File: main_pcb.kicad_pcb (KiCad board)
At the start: 2 copper layers, 56 parts, among them J1 STLink_conn, J10 Conn_01x03_Male, J11 Conn_02x02_Odd_Even, J12 Conn_01x09_Male, J13 Conn_Coaxial, J14 Conn_01x03_Male, J15 USB_conn, J2 Conn_01x04_Male, J3 Conn_02x03_Odd_Even, J4 Conn_02x03_Odd_Even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

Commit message: initial commit
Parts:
- C1, C6, C7, C8, C9: footprint Capacitors_SMD:C_0805_HandSoldering -> LoraWAN_pcb:C_0805_HandSoldering
- C2, C3, C4, C5: footprint Capacitors_SMD:C_0805_HandSoldering -> LoraWAN_pcb:C_0805_HandSoldering; moved to F.Cu
- D1, D3, D4, D5: footprint LEDs:LED_0805_HandSoldering -> LoraWAN_pcb:LED_0805_HandSoldering
- D2: footprint RHF78_footprint:RHF78_052 -> LoraWAN_pcb:RHF78_052
- J1: footprint Pin_Headers:Pin_Header_Straight_1x05_Pitch2.54mm -> LoraWAN_pcb:Pin_Header_Straight_1x05_Pitch2.54mm
- J10, J14, J6, J7: footprint Pin_Headers:Pin_Header_Straight_1x03_Pitch2.54mm -> LoraWAN_pcb:Pin_Header_Straight_1x03_Pitch2.54mm
- J11: footprint Pin_Headers:Pin_Header_Straight_2x02_Pitch2.54mm -> LoraWAN_pcb:Pin_Header_Straight_2x02_Pitch2.54mm
- J12: footprint Pin_Headers:Pin_Header_Straight_1x09_Pitch2.54mm -> LoraWAN_pcb:Pin_Header_Straight_1x09_Pitch2.54mm
- J13: footprint U_FL_smd:U_FL_smd -> LoraWAN_pcb:U_FL_smd
- J15: footprint Connectors:USB_Micro-B -> LoraWAN_pcb:USB_Micro-B
- J2: footprint Pin_Headers:Pin_Header_Straight_1x04_Pitch2.54mm -> LoraWAN_pcb:Pin_Header_Straight_1x04_Pitch2.54mm
- J3, J4: footprint Pin_Headers:Pin_Header_Straight_2x03_Pitch2.54mm -> LoraWAN_pcb:Pin_Header_Straight_2x03_Pitch2.54mm
- J5, J9: footprint Pin_Headers:Pin_Header_Straight_1x01_Pitch2.54mm -> LoraWAN_pcb:Pin_Header_Straight_1x01_Pitch2.54mm
- J8: footprint Pin_Headers:Pin_Header_Straight_1x06_Pitch2.54mm -> LoraWAN_pcb:Pin_Header_Straight_1x06_Pitch2.54mm
- R1, R10, R11, R12, R13, R16, R18, R19, R2, R3, R4, R5, R8, R9: footprint Resistors_SMD:R_0805_HandSoldering -> LoraWAN_pcb:R_0805_HandSoldering
- R14, R15, R6, R7: footprint Resistors_SMD:R_0805_HandSoldering -> LoraWAN_pcb:R_0805_HandSoldering; moved to F.Cu
- R17: footprint Potentiometers:Potentiometer_Trimmer_Bourns_3296W -> LoraWAN_pcb:Potentiometer_Trimmer_Bourns_3296W
- SW1, SW2: footprint Buttons_Switches_SMD:SW_SPST_EVQPE1 -> LoraWAN_pcb:SW_SPST_EVQPE1
- U1: footprint Housings_QFP:LQFP-48_7x7mm_Pitch0.5mm -> LoraWAN_pcb:LQFP-48_7x7mm_Pitch0.5mm; moved to F.Cu
- U2: footprint Housings_SOIC:SOIC-8_3.9x4.9mm_Pitch1.27mm -> LoraWAN_pcb:SOIC-8_3.9x4.9mm_Pitch1.27mm; moved to F.Cu
- U3: footprint TO_SOT_Packages_SMD:SOT-23-6_Handsoldering -> LoraWAN_pcb:SOT-23-6_Handsoldering
- U4: footprint TO_SOT_Packages_SMD:SOT-223-3_TabPin2 -> LoraWAN_pcb:SOT-223-3_TabPin2
- Y1: footprint Crystals:Crystal_HC18-U_Vertical -> LoraWAN_pcb:Crystal_HC18-U_Vertical
- Y2: footprint Crystals:Crystal_AT310_d3.0mm_l10.0mm_Vertical -> LoraWAN_pcb:Crystal_AT310_d3.0mm_l10.0mm_Vertical
- moved Y2 74.5 mm to (174.2, 81.7), turned to 0 degrees
- moved C4 67.8 mm to (170.1, 83.4)
- moved C2 67.2 mm to (170.1, 80.6), turned to 0 degrees
- moved U3 65.3 mm to (107.3, 102.3)
- moved C5 63.2 mm to (163.7, 90.3)
- moved R15 61.4 mm to (175.5, 72.0), turned to 0 degrees
- moved C3 58.3 mm to (159.4, 94.5), turned to 0 degrees
- moved R2 55.3 mm to (158.1, 88.8), turned to 0 degrees
- moved R6 54.7 mm to (169.7, 72.0), turned to 0 degrees
- moved R4 49.6 mm to (169.7, 77.7), turned to 0 degrees
- moved J3 44.9 mm to (150.3, 86.2), turned to 0 degrees
- moved R7 44.4 mm to (158.1, 85.9), turned to 0 degrees
- moved J1 43.4 mm to (138.5, 65.0), turned to 0 degrees
- moved J13 42.9 mm to (125.6, 101.6)
- moved J6 41.6 mm to (147.8, 76.5)
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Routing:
- net GND: track 102.2 -> 0.00 mm, vias 3 -> 0
- net VCC: track 59.6 -> 0.00 mm
- net Net-(J2-Pad3): track 49.7 -> 0.00 mm
- net Net-(J2-Pad2): track 46.1 -> 0.00 mm
- net Net-(D2-Pad23): track 38.2 -> 0.00 mm, vias 1 -> 0
- net Net-(J12-Pad1): track 37.5 -> 0.00 mm
- net Net-(D2-Pad22): track 36.1 -> 0.00 mm, vias 1 -> 0
- net Net-(C4-Pad1): track 34.6 -> 0.00 mm, vias 1 -> 0
- net Net-(J14-Pad2): track 33.0 -> 0.00 mm
- net Net-(C5-Pad1): track 28.8 -> 0.00 mm, vias 1 -> 0
- net /R: track 24.3 -> 0.00 mm, vias 1 -> 0
- net Net-(C2-Pad1): track 20.1 -> 0.00 mm
- net /3v3_STLink: track 14.4 -> 0.00 mm
- net Net-(C3-Pad1): track 14.3 -> 0.00 mm
- net /i2c1_scl: track 13.8 -> 0.00 mm
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
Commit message: work PC
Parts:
- C2, C3, C4, C5, D2, J13, R4: moved to B.Cu
- moved J11 102.5 mm to (73.7, 69.7)
- moved Y2 77.0 mm to (97.2, 80.4), turned to 270 degrees
- moved C4 72.7 mm to (97.9, 75.2), turned to 90 degrees
- moved C5 70.2 mm to (95.2, 75.2), turned to 90 degrees
- moved C2 67.6 mm to (102.8, 75.2), turned to 90 degrees
- moved J3 65.0 mm to (139.5, 150.3)
- moved C3 62.1 mm to (100.4, 75.2), turned to 90 degrees
- moved J6 56.3 mm to (91.6, 80.5)
- moved J7 54.9 mm to (112.9, 122.4)
- moved R4 54.4 mm to (118.3, 95.5)
- moved J1 53.6 mm to (139.7, 118.6)
- moved J9 52.4 mm to (112.2, 97.1)
- moved J13 45.2 mm to (135.9, 57.5)
- moved J10 44.2 mm to (158.2, 41.5)
- moved J4 41.1 mm to (176.4, 110.3)
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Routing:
- net GND: track 0.00 -> 52.7 mm
- net Net-(C5-Pad1): track 0.00 -> 24.4 mm
- net Net-(C4-Pad1): track 0.00 -> 20.5 mm
- net Net-(C3-Pad1): track 0.00 -> 18.7 mm
- net /spi1_mosi: track 0.00 -> 16.6 mm
- net Net-(D1-Pad1): track 0.00 -> 15.8 mm, vias 0 -> 1
- net /spi1_miso: track 0.00 -> 15.7 mm
- net /spi1_nss: track 0.00 -> 15.0 mm
- net /spi1_sck: track 0.00 -> 14.9 mm
- net Net-(C2-Pad1): track 0.00 -> 12.6 mm
- net Net-(D2-Pad20): track 0.00 -> 5.79 mm
- net Net-(D2-Pad15): track 0.00 -> 5.78 mm
- net Net-(D2-Pad16): track 0.00 -> 4.43 mm
- net VCC: track 0.00 -> 3.61 mm

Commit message: work pc - pcbnew
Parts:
- D4, R2, R8, R9: moved to B.Cu
- moved J3 91.0 mm to (122.1, 61.0), turned to 90 degrees
- moved R17 89.8 mm to (92.6, 65.0), turned to 90 degrees
- moved J14 73.8 mm to (91.7, 75.1)
- moved J1 72.4 mm to (119.0, 49.2), turned to 270 degrees
- moved R3 66.5 mm to (135.9, 73.7)
- moved U4 64.6 mm to (122.5, 69.6)
- moved J7 64.3 mm to (113.4, 58.0), turned to 180 degrees
- moved R6 63.3 mm to (107.9, 85.3), turned to 180 degrees
- moved R15 62.4 mm to (113.5, 65.2)
- moved C1 62.0 mm to (92.9, 88.0)
- moved R9 59.8 mm to (96.8, 61.2), turned to 270 degrees
- moved J15 59.7 mm to (138.9, 64.2), turned to 90 degrees
- moved R10 59.6 mm to (91.6, 84.4), turned to 270 degrees
- moved J2 58.4 mm to (140.9, 71.9)
- moved J12 54.9 mm to (100.4, 111.2), turned to 90 degrees
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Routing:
- net GND: track 52.7 -> 183.5 mm, vias 0 -> 5
- net VCC: track 3.61 -> 111.9 mm, vias 0 -> 4
- net Net-(J14-Pad2): track 0.00 -> 30.0 mm
- net /R: track 0.00 -> 29.5 mm
- net /UART_FW: track 0.00 -> 26.7 mm
- net Net-(R18-Pad2): track 0.00 -> 20.5 mm
- net /BOOT1: track 0.00 -> 18.7 mm
- net Net-(R19-Pad1): track 0.00 -> 18.4 mm
- net /i2c1_sda: track 0.00 -> 14.0 mm
- net /AMS1117_3v3: track 0.00 -> 9.90 mm
- net Net-(R16-Pad2): track 0.00 -> 9.54 mm
- net Net-(C8-Pad2): track 0.00 -> 9.27 mm
- net Net-(D2-Pad14): track 0.00 -> 8.60 mm, vias 0 -> 1
- net Net-(D2-Pad32): track 0.00 -> 8.55 mm
- net Net-(J11-Pad2): track 0.00 -> 7.71 mm
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
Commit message: work pc pcbnew
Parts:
- R3: moved to B.Cu
- moved J1 63.0 mm to (88.0, 104.0), turned to 90 degrees
- moved J6 44.8 mm to (90.9, 95.1), turned to 0 degrees
- moved J7 42.0 mm to (93.6, 95.1), turned to 0 degrees
- moved J10 39.9 mm to (96.2, 95.1), turned to 0 degrees
- moved J2 7.09 mm to (140.8, 79.0), turned to 180 degrees
- moved D5 1.57 mm to (132.9, 92.9), turned to 270 degrees
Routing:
- net Net-(R12-Pad1): track 0.00 -> 25.6 mm, vias 0 -> 2
- net GND: track 183.5 -> 176.4 mm
- net VCC: track 111.9 -> 115.8 mm
- net /UART_FW: track 26.7 -> 30.2 mm
- net /BOOT0: track 0.00 -> 2.77 mm
- net Net-(J2-Pad3): track 7.19 -> 5.20 mm
- net Net-(J2-Pad2): track 3.91 -> 5.21 mm
- net /TX_fw: vias 1 -> 0

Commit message: board trace is finished
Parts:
- removed R12: 100K, LoraWAN_pcb:R_0805_HandSoldering
- J12: value Conn_01x09_Male -> Conn_01x01_Male; footprint LoraWAN_pcb:Pin_Header_Straight_1x09_Pitch2.54mm -> LoraWAN_pcb:Pin_Header_Straight_1x01_Pitch2.54mm
- J4: value Conn_02x03_Odd_Even -> Conn_01x03_Male; footprint LoraWAN_pcb:Pin_Header_Straight_2x03_Pitch2.54mm -> LoraWAN_pcb:Pin_Header_Straight_1x03_Pitch2.54mm
- R11: value 100K -> 5K
- moved J12 52.4 mm to (112.8, 60.3), turned to 0 degrees
- moved J6 45.1 mm to (134.6, 83.7)
- moved J7 45.0 mm to (137.1, 83.6)
- moved J1 44.9 mm to (131.4, 92.5)
- moved J10 44.9 mm to (139.6, 83.6)
- moved D5 29.9 mm to (107.7, 76.8), turned to 0 degrees
- moved R13 26.0 mm to (107.8, 78.8), turned to 0 degrees
- moved J2 22.3 mm to (128.5, 60.4), turned to 270 degrees
- moved J4 17.2 mm to (139.8, 101.3), turned to 180 degrees
- moved J3 16.9 mm to (138.5, 65.2), turned to 0 degrees
- moved R18 14.6 mm to (130.4, 79.3)
- moved R19 14.5 mm to (130.4, 77.2)
- moved D3 13.8 mm to (123.6, 91.8)
- moved J15 12.9 mm to (138.6, 77.2)
- moved SW2 7.25 mm to (96.3, 89.3)
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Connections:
- J4 pad 1: VCC -> Net-(J4-Pad1)
- J4 pad 2: VCC -> Net-(J4-Pad2)
- J4 pad 3: /BOOT0 -> Net-(J4-Pad3)
- R11 pad 1: /BOOT1 -> Net-(R11-Pad1)
- R11 pad 2: Net-(R11-Pad2) -> GND
- U1 pad 1: /3VB -> Net-(J12-Pad1)
- U1 pad 20: Net-(R11-Pad2) -> Net-(R11-Pad1)
- U1 pad 21: Net-(J12-Pad3) -> Net-(U1-Pad21)
- U1 pad 22: Net-(J12-Pad4) -> Net-(U1-Pad22)
- U1 pad 25: Net-(J12-Pad8) -> Net-(J4-Pad1)
- U1 pad 26: Net-(J12-Pad7) -> Net-(J4-Pad2)
- U1 pad 27: Net-(J12-Pad6) -> Net-(J4-Pad3)
- U1 pad 28: Net-(J12-Pad5) -> Net-(U1-Pad28)
- U1 pad 44: Net-(R12-Pad1) -> GND
- U1 pad 45: Net-(J12-Pad2) -> Net-(U1-Pad45)
- U1 pad 46: Net-(J12-Pad1) -> Net-(U1-Pad46)
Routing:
- net /R: track 29.5 -> 97.0 mm
- net VCC: track 115.8 -> 159.9 mm, vias 4 -> 6
- net GND: track 176.4 -> 219.4 mm
- net /3v3_STLink: track 0.00 -> 41.3 mm
- net Net-(D2-Pad27): track 0.00 -> 35.3 mm
- net Net-(J4-Pad1): track 0.00 -> 35.2 mm, vias 0 -> 1
- net Net-(J10-Pad3): track 0.00 -> 33.3 mm, vias 0 -> 1
- net Net-(J4-Pad2): track 0.00 -> 26.9 mm, vias 0 -> 1
- net Net-(J12-Pad1): track 0.00 -> 26.1 mm, vias 0 -> 2
- net Net-(R12-Pad1): track 25.6 -> 0.00 mm, vias 2 -> 0
- net Net-(J4-Pad3): track 0.00 -> 25.3 mm, vias 0 -> 1
- net Net-(J10-Pad2): track 0.00 -> 24.6 mm, vias 0 -> 2
- net Net-(C8-Pad2): track 9.27 -> 31.4 mm, vias 0 -> 2
- net /AMS1117_3v3: track 9.90 -> 31.7 mm
- net /BOOT1: track 18.7 -> 0.00 mm
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
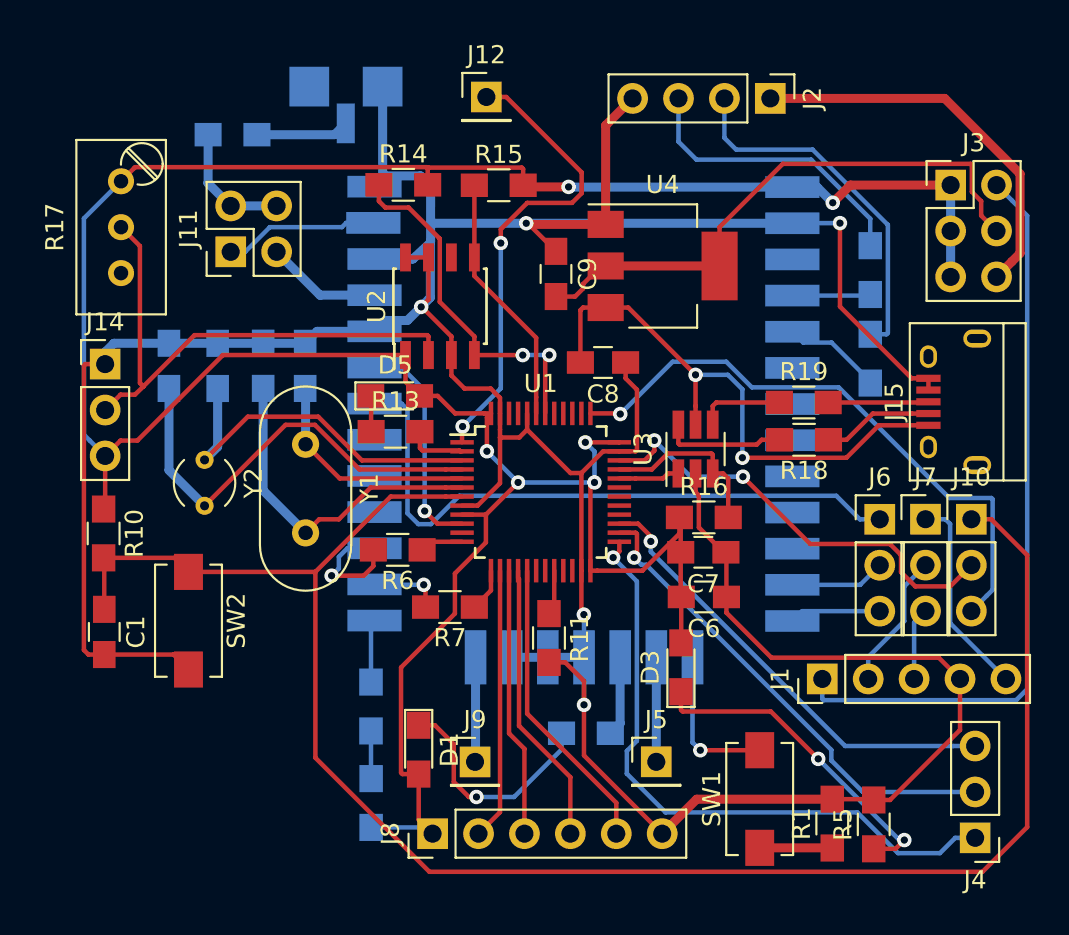
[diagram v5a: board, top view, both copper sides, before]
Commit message: add new pin header 3x3
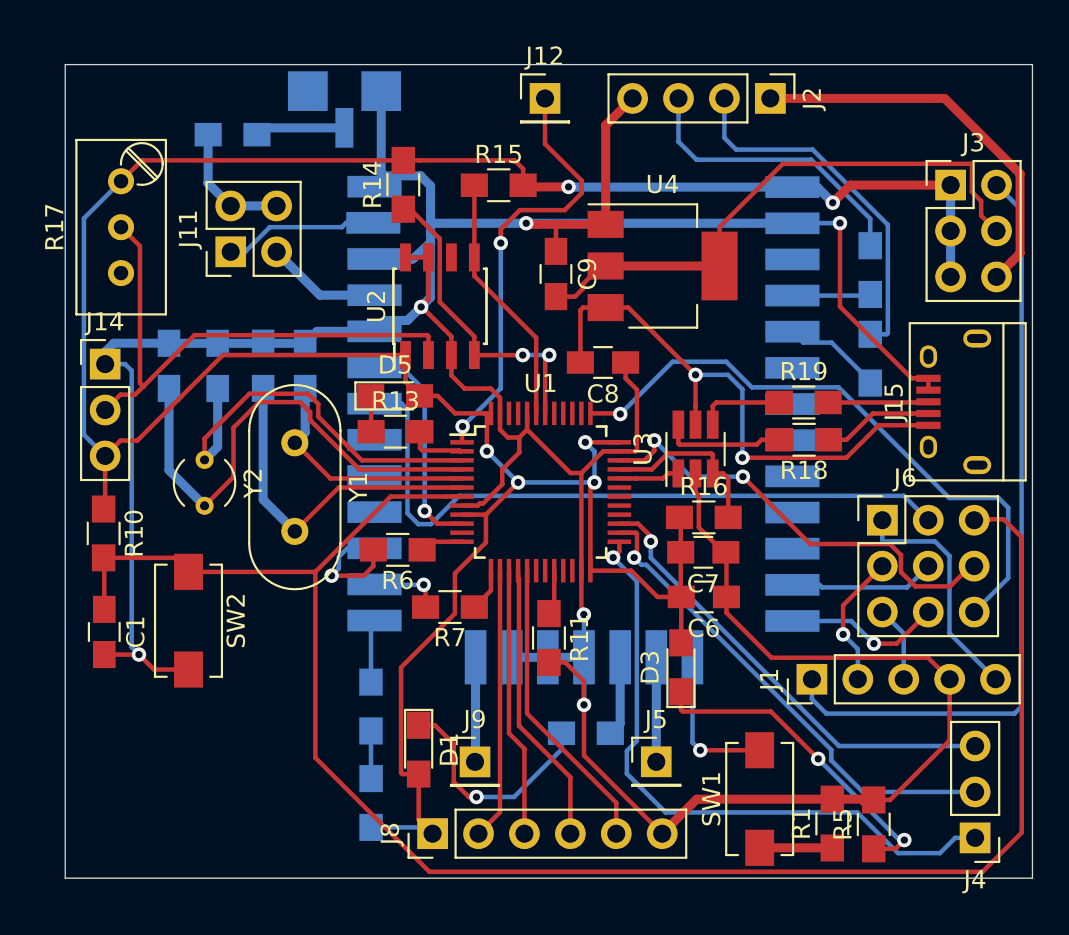
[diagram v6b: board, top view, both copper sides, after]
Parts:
- removed J10, J7: Conn_01x03_Male, LoraWAN_pcb:Pin_Header_Straight_1x03_Pitch2.54mm
- J6: value Conn_01x03_Male -> stlink_conn; footprint LoraWAN_pcb:Pin_Header_Straight_1x03_Pitch2.54mm -> LoraWAN_pcb:PinHeader_3x03_P2.54mm_Vertical
- moved J12 3.25 mm to (116.0, 60.4)
- moved Y1 0.60 mm to (102.2, 79.4)
- moved J1 0.57 mm to (130.8, 92.5)
- moved J13 0.26 mm to (104.9, 60.0)
- moved J6 0.15 mm to (134.7, 83.7)
- turned R14 to 90 degrees
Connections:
- J6 pad 1: Net-(D2-Pad27) -> Net-(J1-Pad5)
- J6 pad 2: Net-(D2-Pad12) -> Net-(J1-Pad2)
- J6 pad 3: Net-(D2-Pad13) -> Net-(J1-Pad3)
- U1 pad 34: Net-(J10-Pad2) -> Net-(J6-Pad8)
- U1 pad 37: Net-(J10-Pad3) -> Net-(J6-Pad9)
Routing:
- net Net-(J6-Pad9): track 0.00 -> 34.2 mm, vias 0 -> 1
- net Net-(J10-Pad3): track 33.3 -> 0.00 mm, vias 1 -> 0
- net Net-(J6-Pad8): track 0.00 -> 24.6 mm, vias 0 -> 2
- net Net-(J10-Pad2): track 24.6 -> 0.00 mm, vias 2 -> 0
- net Net-(D2-Pad13): track 5.06 -> 8.76 mm, vias 0 -> 1
- net Net-(C5-Pad1): track 24.4 -> 27.3 mm
- net Net-(D2-Pad27): track 35.3 -> 38.0 mm
- net /i2c1_scl: track 19.8 -> 17.1 mm
- net Net-(C4-Pad1): track 20.5 -> 22.6 mm
- net Net-(D2-Pad12): track 5.93 -> 8.06 mm
- net Net-(J12-Pad1): track 26.1 -> 24.1 mm
- net Net-(J1-Pad5): track 11.3 -> 13.1 mm
- net VCC: track 159.9 -> 158.2 mm
- net GND: track 219.4 -> 217.8 mm, vias 5 -> 6
- net /3v3_STLink: track 41.3 -> 42.6 mm
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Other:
- board outline added: 53.5 x 45 mm

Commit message: pcbnew complited
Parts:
- D2: value RHF78-052 -> RHF78-052-RF_Module
